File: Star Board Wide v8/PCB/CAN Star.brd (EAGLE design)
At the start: 114.3 x 74.9 mm, 12 parts

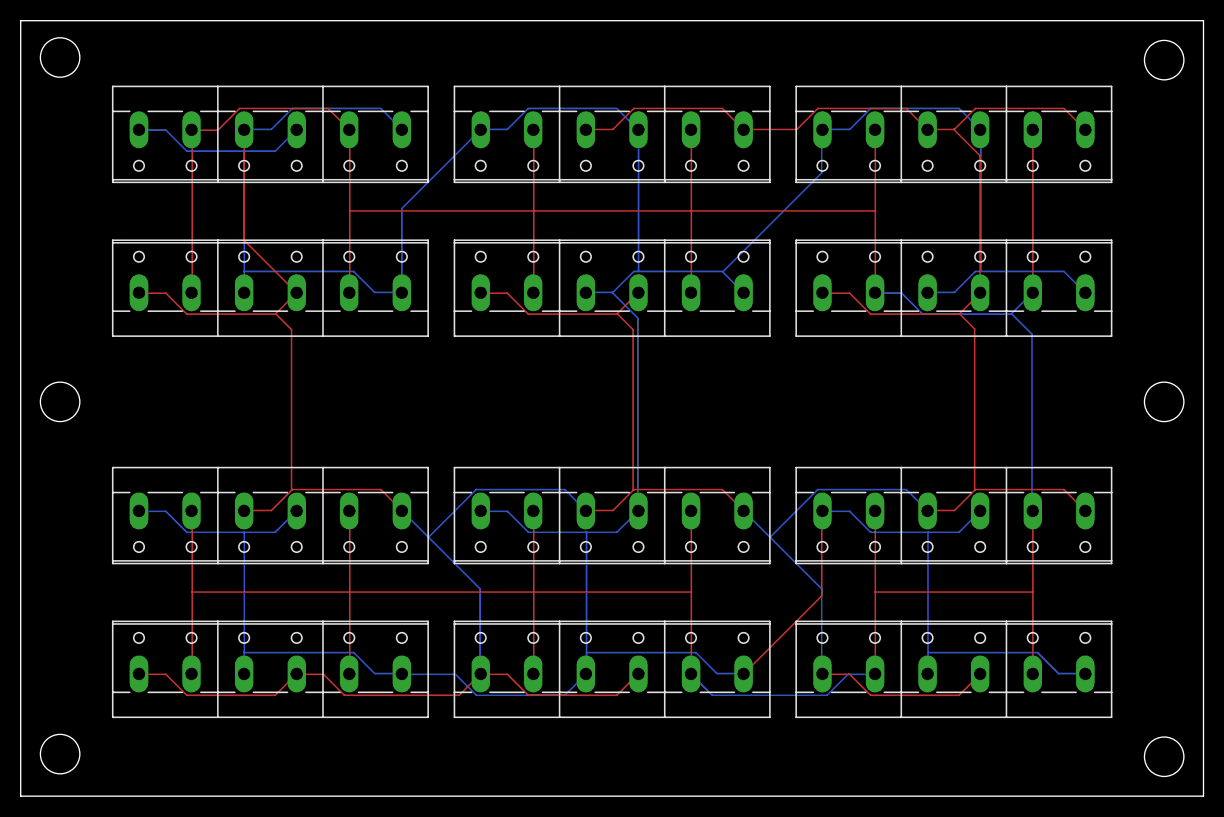
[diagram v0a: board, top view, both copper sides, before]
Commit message: Updated with ground pour
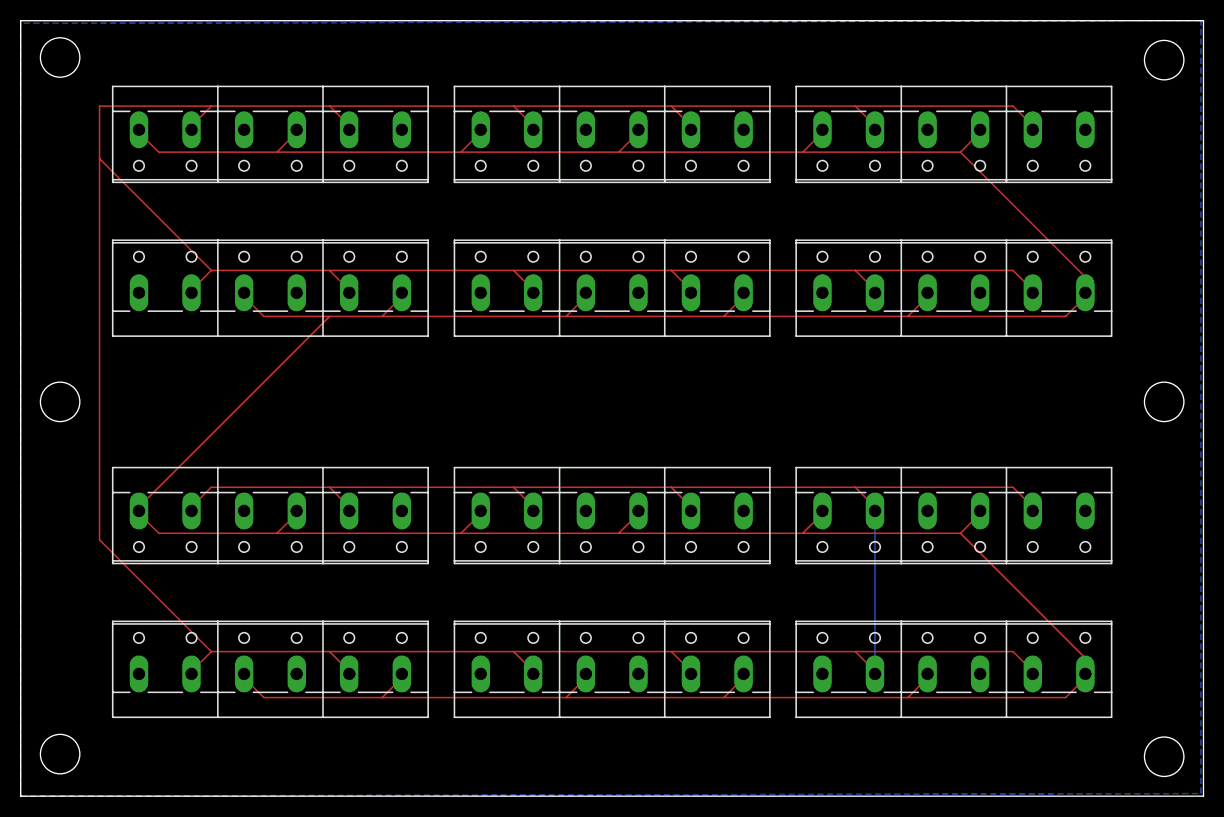
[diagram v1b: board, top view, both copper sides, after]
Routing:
- net GND: track 404.0 -> 0.00 mm
- net Y(H): track 376.9 -> 481.1 mm
- net G(L): track 379.4 -> 445.8 mm
- added copper zone on layer 16, net GND
